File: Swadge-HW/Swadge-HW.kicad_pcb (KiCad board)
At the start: 2 copper layers, 136 x 75 mm, 93 parts, among them J1 SAO, J2 PJ-307C, J3 PGM, P1 USB_C_Plug_USB2.0, Q1 Q_PMOS_GSD, SW1 YTS-D003-1A, SW2 YTS-D003-1A, SW3 YTS-D003-1A, SW4 YTS-D003-1A, SW5 YTS-D003-1A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

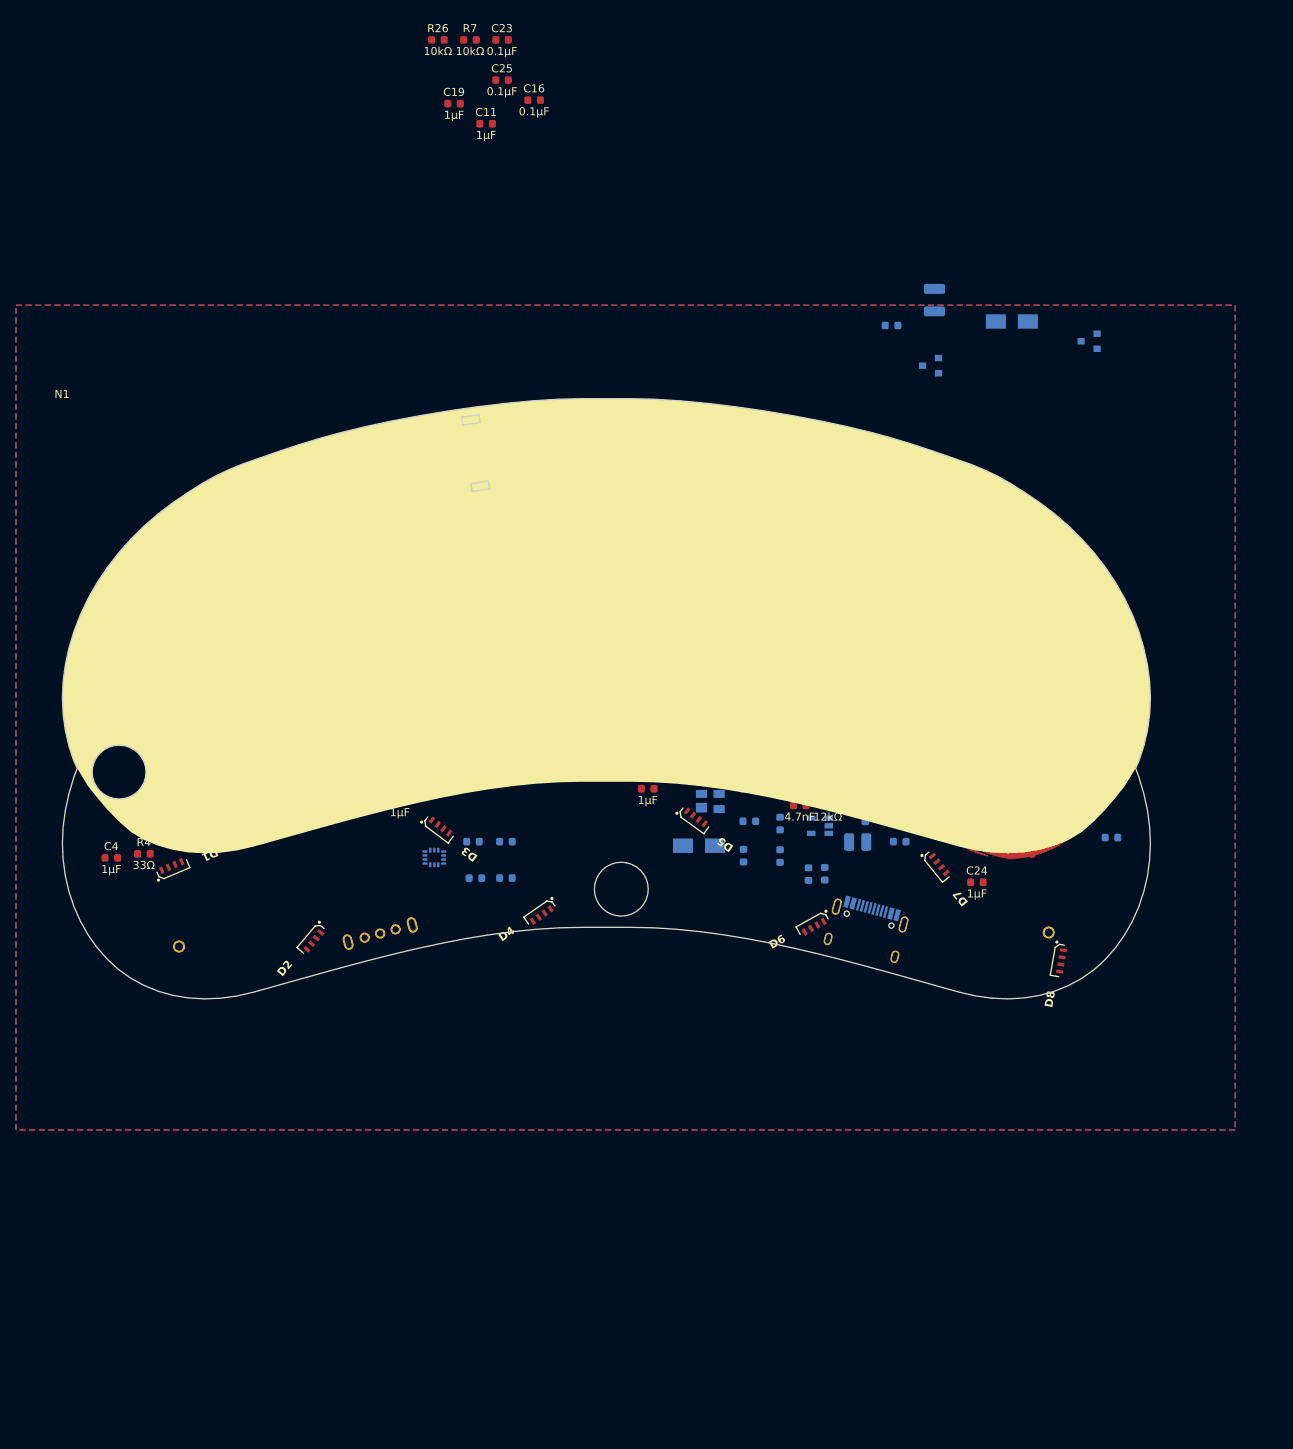
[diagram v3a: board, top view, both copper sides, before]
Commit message: Layout 0.7
Is endless screaming an option for a description?
10lbs of swadge in a 5lb layout. Moved some USB peripherals after plagiarizing from the gunship layout, more attempts to work myself out of the corner of my own creation. Need to consider moving all the TFT ICs.
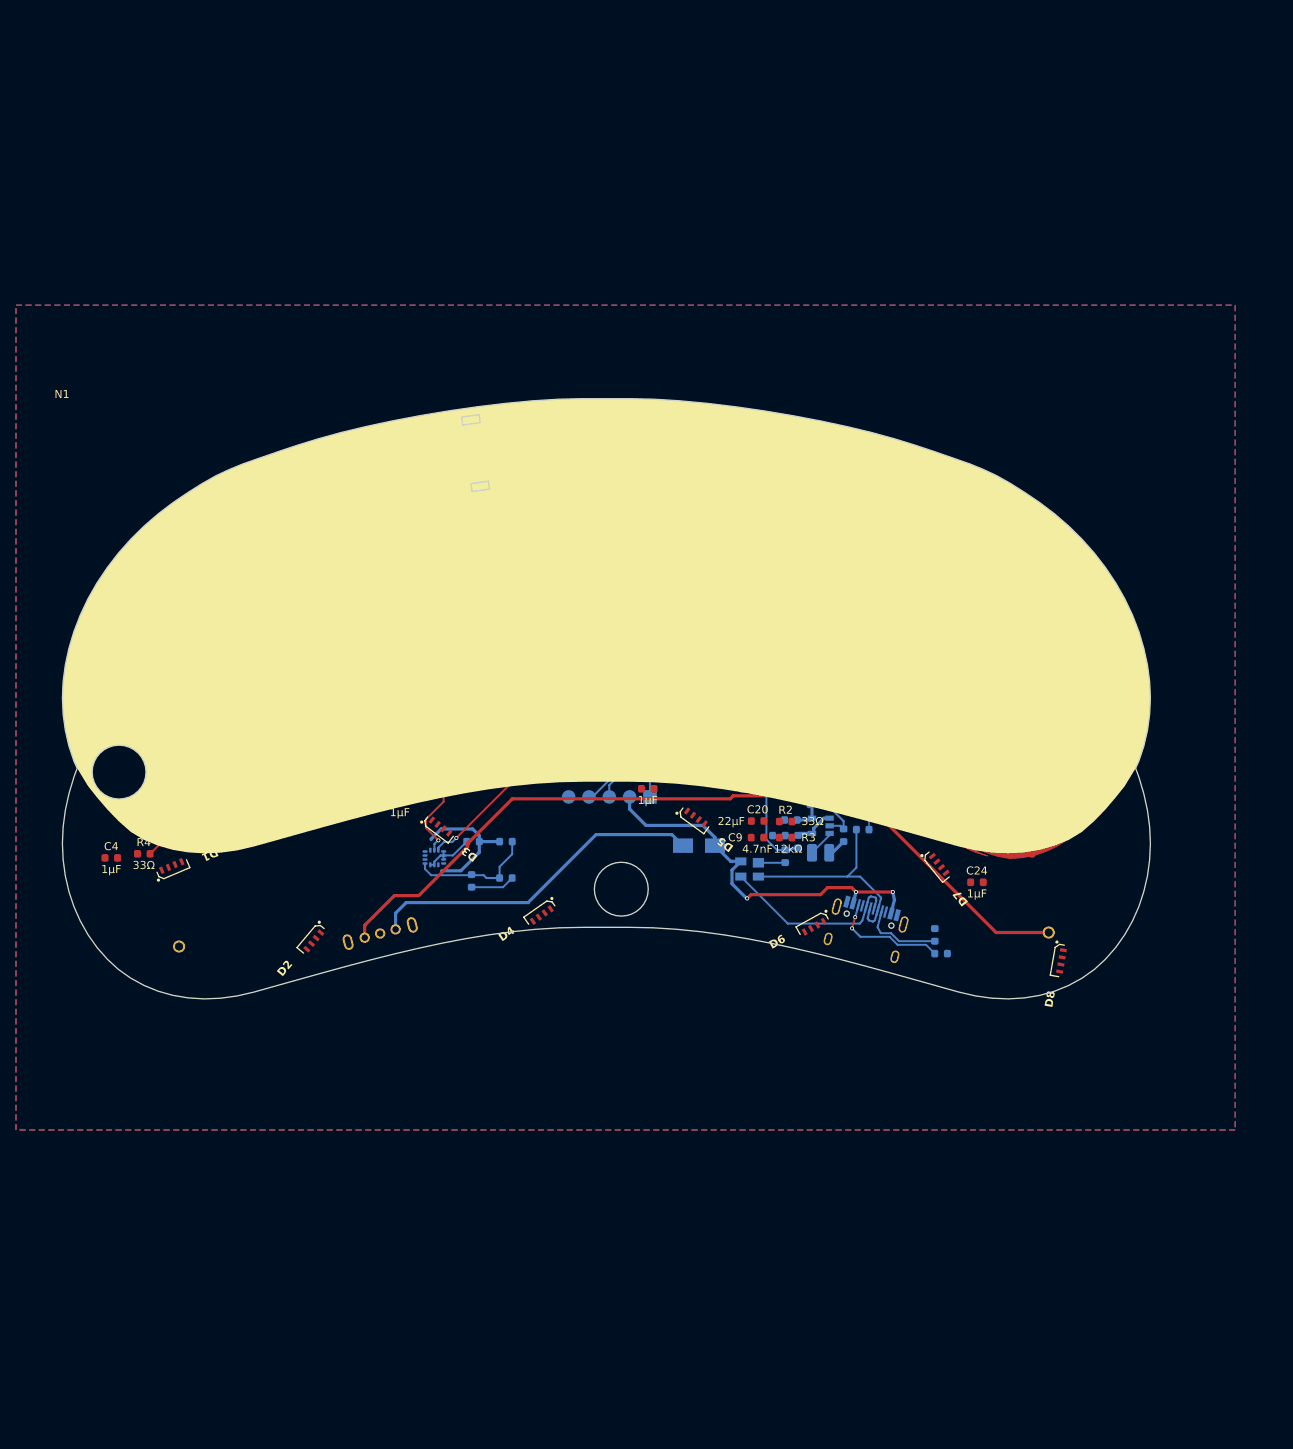
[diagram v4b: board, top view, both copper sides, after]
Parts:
- C11, C16, C19, C23, C25, R26, R7: moved to B.Cu
- RV1: value R_Potentiometer_US_SMD -> (none)
- U7: value GENERIC_LDO_2.8 -> (none)
- moved R7 80.5 mm to (181.4, 82.0), turned to 90 degrees
- moved U7 72.7 mm to (144.8, 86.9), turned to 0 degrees
- moved C11 72.5 mm to (179.6, 85.3)
- moved C23 65.6 mm to (144.6, 82.8)
- moved C16 62.8 mm to (147.8, 87.6), turned to -90 degrees
- moved C25 56.6 mm to (144.8, 78.7)
- moved R26 50.7 mm to (143.3, 66.3), turned to 90 degrees
- moved C19 48.7 mm to (143.5, 72.6)
- moved L1 42.4 mm to (173.9, 88.9), turned to 180 degrees
- moved D10 41.4 mm to (180.3, 88.9), turned to 0 degrees
- moved C22 39.1 mm to (169.4, 88.9)
- moved J3 32.3 mm to (155.4, 112.3)
- moved R17 28.1 mm to (186.4, 112.8)
- moved Q1 27.3 mm to (177.3, 82.2)
- moved R27 17.6 mm to (191.8, 131.8), turned to 180 degrees
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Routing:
- net SCL: track 0.00 -> 121.5 mm, vias 0 -> 4
- net +3V3: track 0.00 -> 109.6 mm, vias 0 -> 2
- net BATTPLUS: track 0.00 -> 101.1 mm
- net SDA: track 0.00 -> 100.2 mm, vias 0 -> 2
- net LED: track 0.00 -> 88.2 mm, vias 0 -> 1
- net TFTATP: track 0.00 -> 82.4 mm, vias 0 -> 6
- net BTN_7: track 0.00 -> 70.1 mm, vias 0 -> 5
- net RX: track 0.00 -> 64.9 mm, vias 0 -> 2
- net TOUCH_1: track 0.00 -> 62.9 mm, vias 0 -> 2
- net TX: track 0.00 -> 61.8 mm, vias 0 -> 2
- net BTN_6: track 0.00 -> 59.7 mm, vias 0 -> 2
- net TOUCH_2: track 0.00 -> 59.1 mm, vias 0 -> 2
- net GPIO40: track 0.00 -> 58.2 mm, vias 0 -> 2
- net TFT_LEDA: track 0.00 -> 56.0 mm, vias 0 -> 3
- net BTN_1: track 0.00 -> 54.4 mm, vias 0 -> 2
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- added copper zone on B.Cu, net GND
- added copper zone on F.Cu, net GND
- removed copper zone on B.Cu, net (none)
- removed copper zone on F.Cu, net (none)

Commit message: Layout 0.9
for review
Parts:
- moved J2 65.5 mm to (89.8, 88.7), turned to -120 degrees
- moved D10 33.2 mm to (150.2, 74.8)
- moved U6 33.2 mm to (160.9, 112.6)
- moved C11 33.2 mm to (146.4, 85.2), turned to 180 degrees
- moved L1 30.5 mm to (149.0, 71.3), turned to 0 degrees
- moved R7 29.2 mm to (152.4, 79.0), turned to 0 degrees
- moved Q1 29.2 mm to (148.4, 78.5)
- moved C12 26.9 mm to (158.2, 112.7), turned to 90 degrees
- moved C10 26.7 mm to (158.9, 110.3)
- moved C13 24.7 mm to (161.1, 115.5)
- moved C22 24.6 mm to (152.3, 71.2), turned to -90 degrees
- moved R8 17.0 mm to (154.3, 115.7)
- moved C1 11.0 mm to (157.2, 69.3), turned to 180 degrees
- moved R18 7.47 mm to (149.7, 88.7), turned to -90 degrees
- moved C4 5.58 mm to (92.7, 123.1), turned to -90 degrees
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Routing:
- net +3V3: track 109.6 -> 386.3 mm, vias 2 -> 13
- net BTN_2: track 1.56 -> 112.6 mm, vias 1 -> 5
- net BTN_3: track 1.77 -> 98.3 mm, vias 1 -> 5
- net BTN_4: track 1.91 -> 97.0 mm, vias 1 -> 5
- net BTN_1: track 54.4 -> 141.6 mm, vias 2 -> 4
- net BTN_5: track 4.00 -> 76.5 mm, vias 1 -> 3
- net TFTATP: track 82.4 -> 11.9 mm, vias 6 -> 0
- net SNODE: track 6.81 -> 70.5 mm, vias 0 -> 2
- net TOUCH_5: track 16.7 -> 63.7 mm, vias 2 -> 0
- net Net-(D6-OUT): track 0.00 -> 39.0 mm, vias 0 -> 2
- net TFT_LEDA: track 56.0 -> 20.0 mm, vias 3 -> 1
- net MIC: track 23.3 -> 57.0 mm, vias 3 -> 4
- net SCL: track 121.5 -> 88.9 mm
- net SDA: track 100.2 -> 71.0 mm
- net Net-(D4-OUT): track 0.00 -> 29.0 mm
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
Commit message: Fix DRC things
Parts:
- RV1: value (none) -> R_Potentiometer_US_SMD
- U7: value (none) -> GENERIC_LDO_2.8
- moved R14 1.57 mm to (182.0, 117.9)
- moved C17 0.86 mm to (154.8, 110.5), turned to 90 degrees
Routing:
- net GND: track 48.4 -> 55.8 mm, vias 284 -> 308
- net TFT_RS: track 48.9 -> 46.0 mm, vias 5 -> 3
- net +3V3: track 386.3 -> 388.4 mm, vias 13 -> 14
- net USB_D-: track 47.7 -> 49.3 mm
- net Net-(P1-DN1): track 28.1 -> 26.6 mm
- net VMON: track 53.0 -> 54.2 mm
- net TOUCH_5: track 63.7 -> 64.5 mm
- net Net-(U4-Top_Left): track 7.33 -> 7.19 mm, vias 2 -> 1

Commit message: update from changes made by charlesl pre-order
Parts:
- R18, R6: value 47kΩ -> 10kΩ
- moved R18 24.8 mm to (149.0, 63.9), turned to 0 degrees
- moved C21 22.5 mm to (147.3, 66.2), turned to -90 degrees
- moved U10 21.6 mm to (148.9, 65.8), turned to 0 degrees
- moved R6 20.9 mm to (149.6, 68.4), turned to 0 degrees
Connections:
- R18 pad 1: SCL -> +3V3
- R18 pad 2: +3V3 -> SDA
- R6 pad 1: +3V3 -> SCL
- R6 pad 2: SDA -> +3V3
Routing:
- net SDA: track 70.9 -> 93.7 mm, vias 2 -> 4
- net GPIO42: track 36.5 -> 28.7 mm, vias 1 -> 2
- net BTN_8: track 66.1 -> 60.3 mm, vias 3 -> 5
- net +3V3: track 388.4 -> 393.1 mm, vias 14 -> 16
- net SCL: track 88.9 -> 84.6 mm, vias 4 -> 3
- net GND: track 55.8 -> 58.2 mm, vias 308 -> 375
- net BTN_1: track 141.6 -> 142.7 mm
- net RX: track 52.6 -> 52.0 mm
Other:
- board text added: "BATT"
- board text added: "GND RX TX 5V PGM"
- board text added: "Super-2025-Swadge-HW rev -"
- board text added: "USB"
